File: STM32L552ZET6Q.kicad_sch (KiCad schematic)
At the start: 25 parts, among them SW501 MCU_RST, U501 STM32L552ZET6Q, Y501 32.768kHz, 1.2pF, Y502 16MHz, 7pF

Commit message: i dont know what changed. dont ask me.
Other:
- note added: "this is to power external usb hub"
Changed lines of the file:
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@@
+		)
+	)
+	(text "this is to power external usb hub"
+		(exclude_from_sim no)
+		(at 36.068 16.764 0)
+		(effects
+			(font
+				(size 1.27 1.27)
+			)
 		)
 	)

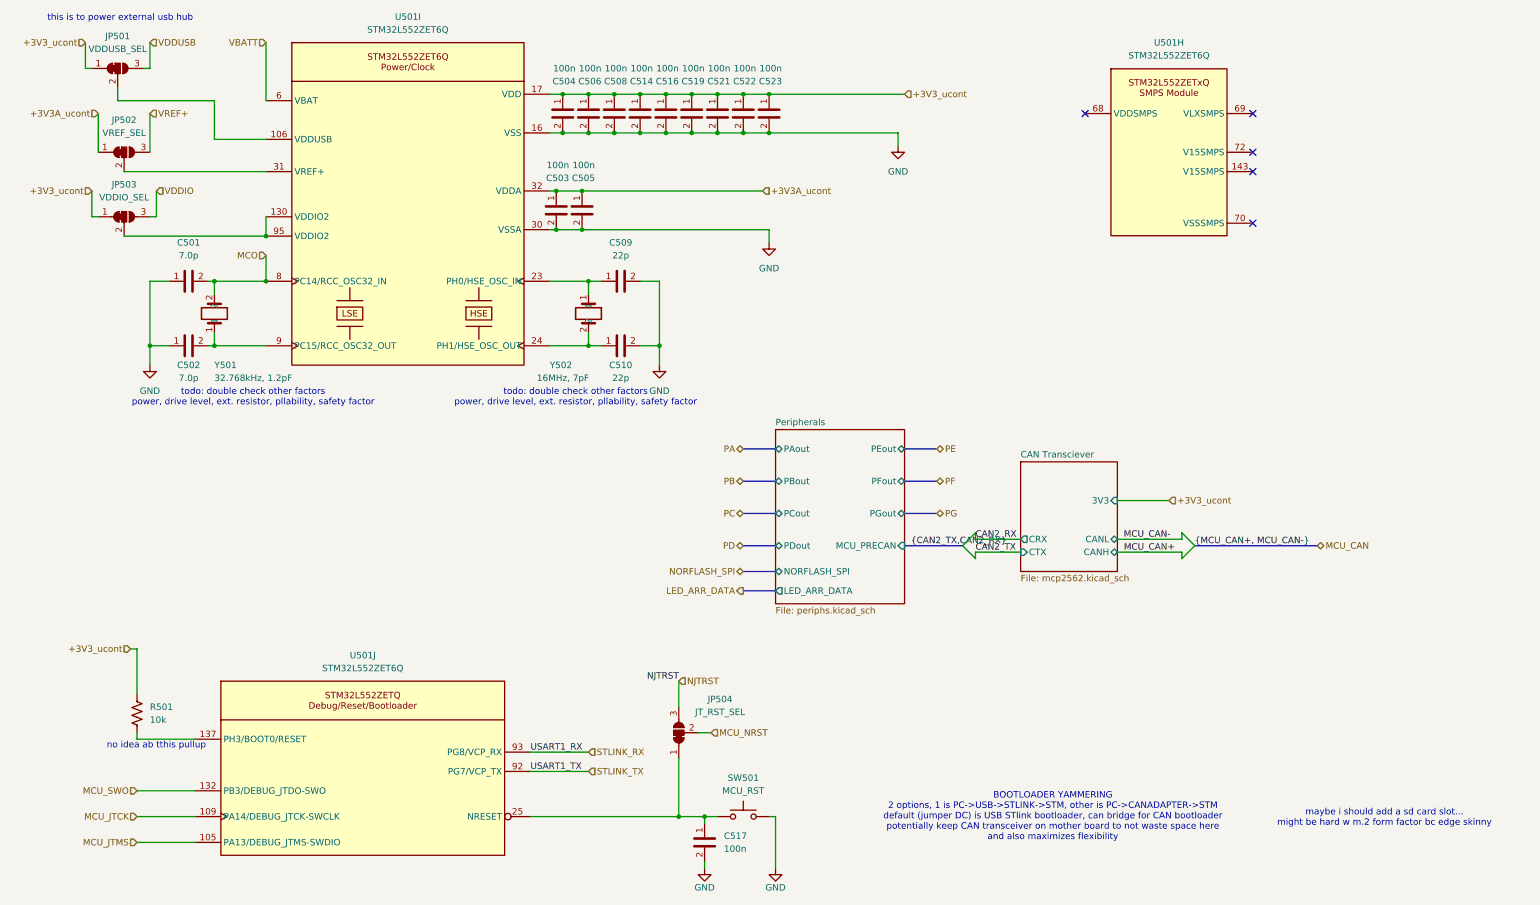
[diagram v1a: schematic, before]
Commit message: small schematic changes, need to reroute
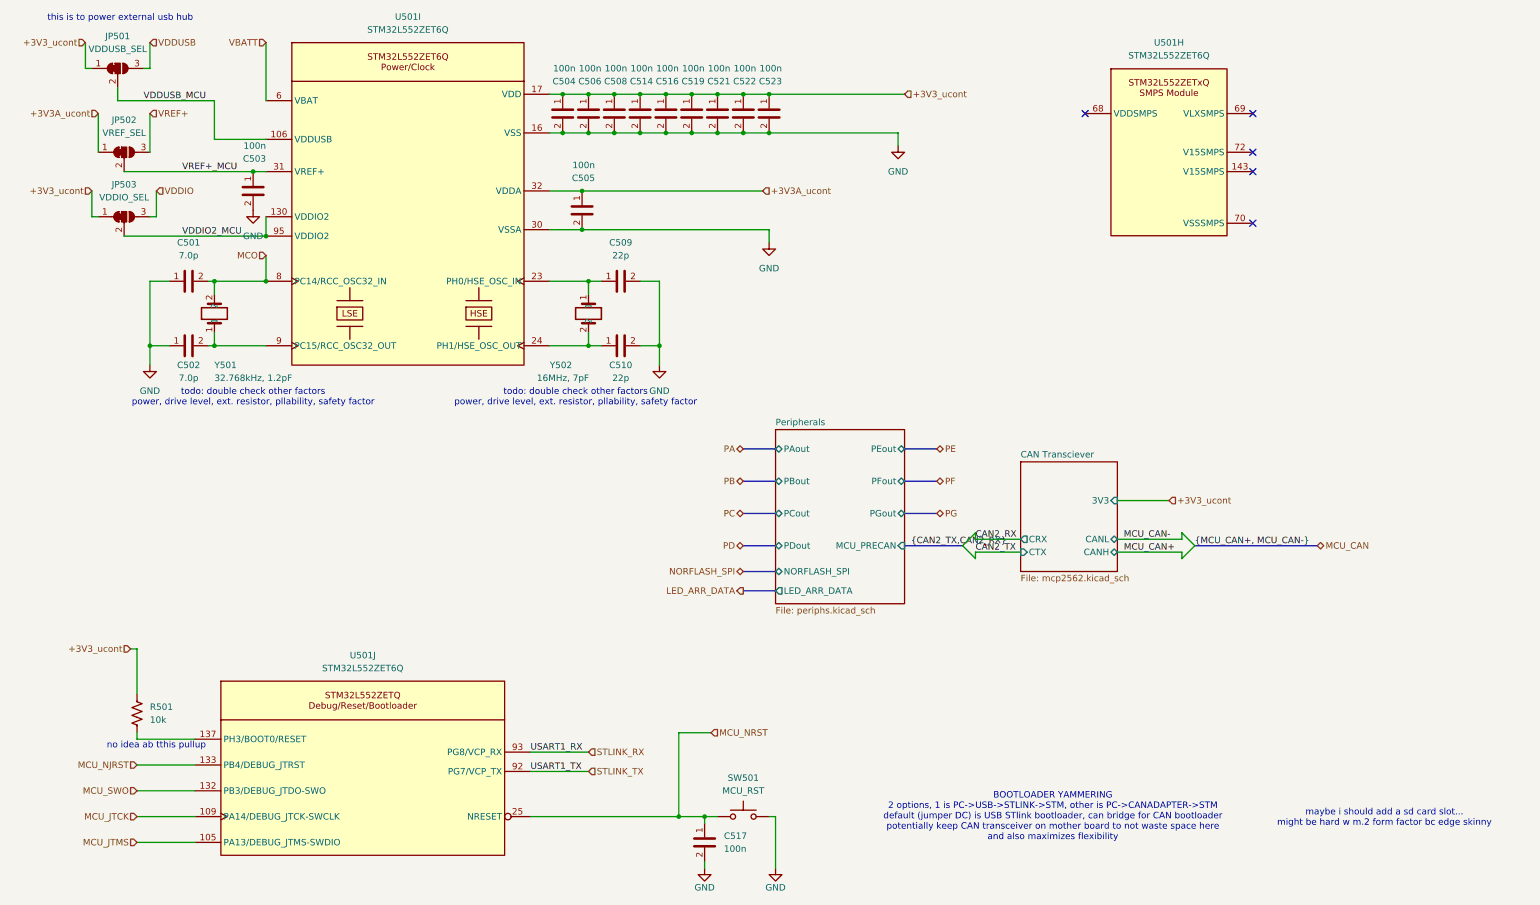
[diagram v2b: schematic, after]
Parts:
- removed JP504: JT_RST_SEL, Jumper:SolderJumper-3_P1.3mm_Bridged2Bar12_Pad1.0x1.5mm_NumberLabels, symbol Jumper:SolderJumper_3_Bridged12
- removed unit 10 of U501
- added unit 10 of U501
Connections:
- net +3V3A_ucont: no longer C503.1
- net MCU_JTCK: now also U501.109 (PA14/DEBUG_JTCK-SWCLK)
- net MCU_JTMS: now also U501.105 (PA13/DEBUG_JTMS-SWDIO)
- net MCU_NRST: now also C517.1, SW501.2, U501.25 (NRESET)
- net MCU_SWO: now also U501.132 (PB3/DEBUG_JTDO-SWO)
- net STLINK_RX: now also U501.93 (PG8/VCP_RX)
- net STLINK_TX: now also U501.92 (PG7/VCP_TX)
- net VDDIO2_MCU: now reaches JP503.2 (C), U501.130 (VDDIO2), U501.95 (VDDIO2)
- net VREF+_MCU: now reaches JP502.2 (C), U501.31 (VREF+)
- net VREF+_MCU: now also C503.1
- net VDDUSB_MCU: now reaches JP501.2 (C), U501.106 (VDDUSB)
- net at R501.1: now also U501.137 (PH3/BOOT0/RESET)
- new net MCU_NJRST: U501.133 (PB4/DEBUG_JTRST)
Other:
- moved on the sheet: C503
